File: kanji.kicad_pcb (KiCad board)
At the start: 2 copper layers, 105.3 x 70.8 mm, 35 parts, among them J3 E-Ink, Q1 AO3400A, U1 BH1750FVI-TR, U3 SHT4x, U4 XIAO-ESP32-S3-SMD

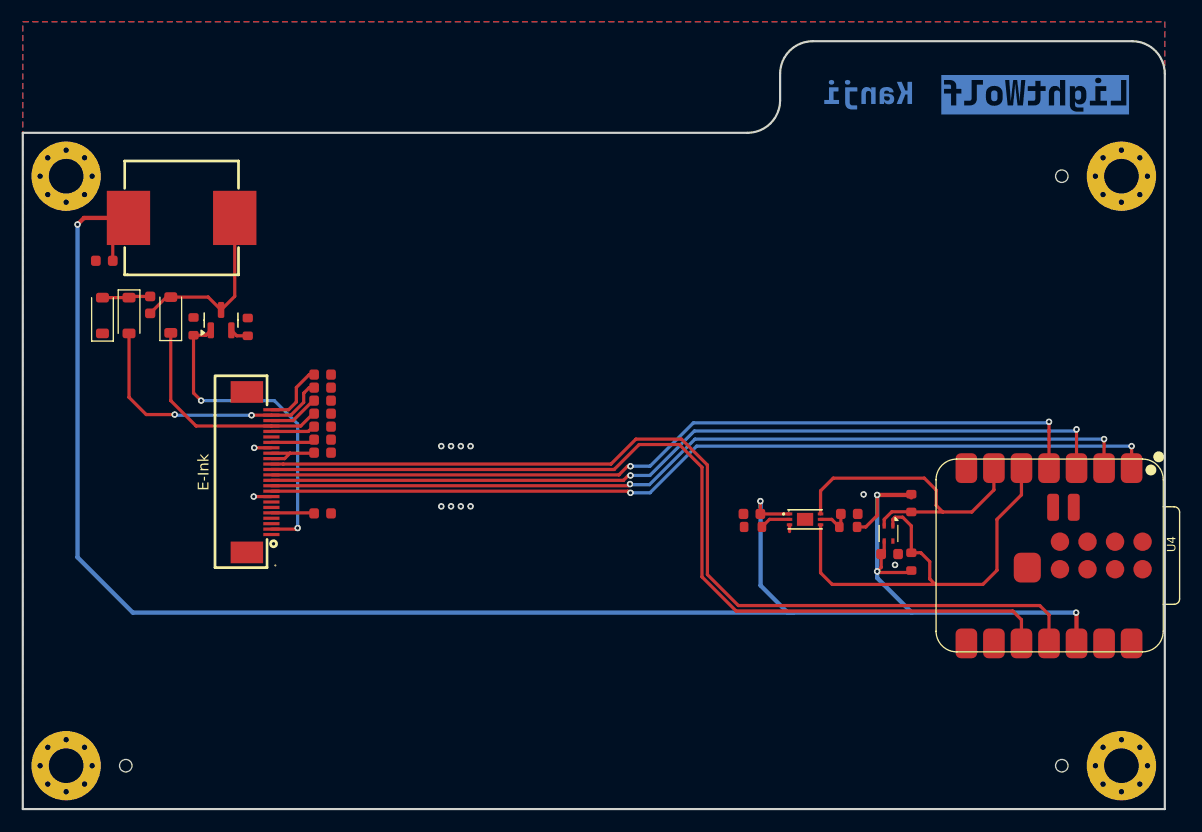
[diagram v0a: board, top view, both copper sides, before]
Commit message: feat: add case and update readme
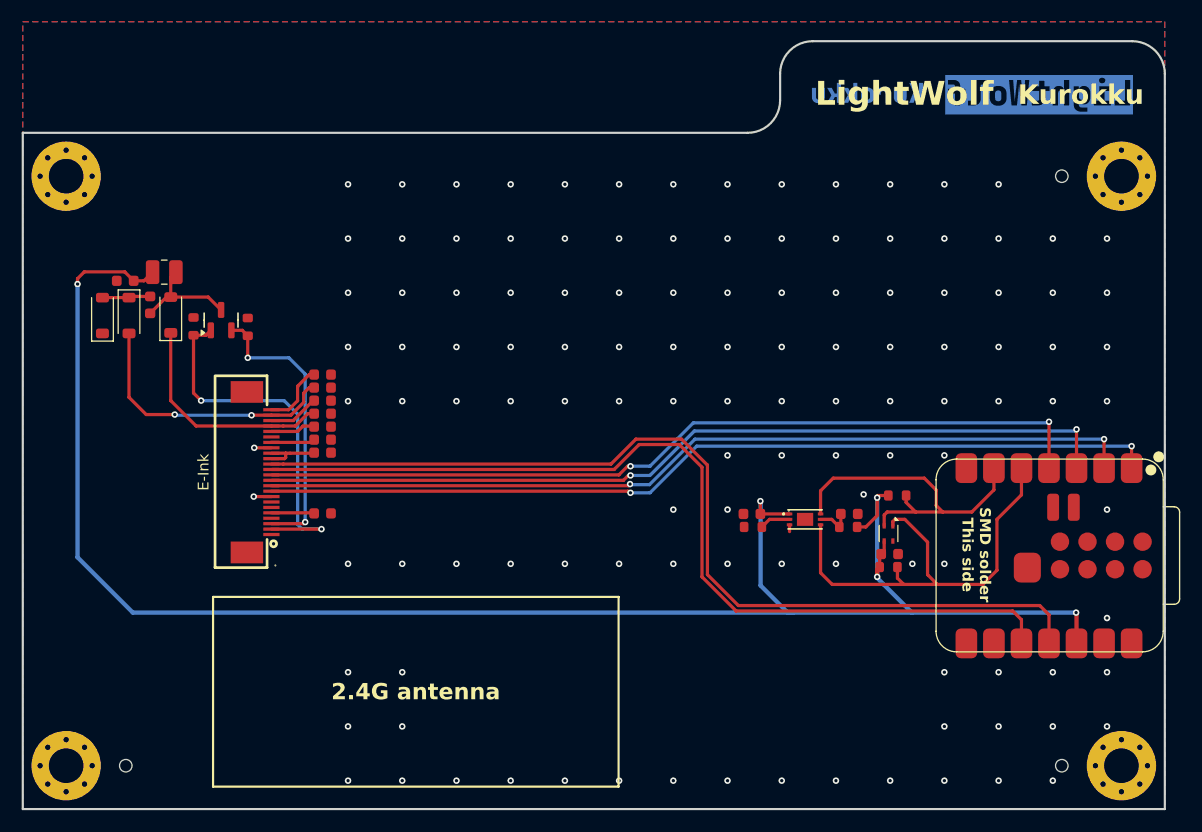
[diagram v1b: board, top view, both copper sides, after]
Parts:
- removed L1: CYL104R-47UH, easyeda2kicad:IND-SMD_L10.5-W10.5
- added L2: 10uH, Inductor_SMD:L_1008_2520Metric, F.Cu at (112.4, 75.8)
- R5: value 2.2Ω -> 3Ω
- R6: value 1MΩ -> 10kΩ
- moved C15 2.67 mm to (108.8, 76.6)
- moved R10 2.16 mm to (179.2, 103.0), turned to 0 degrees
- moved R9 1.48 mm to (180.0, 96.4), turned to 0 degrees
- turned R5 to -90 degrees
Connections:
- Q1 pad 2: Net-(Q1-S) -> /RDSE
- R5 pad 1: Net-(Q1-S) -> GND
- R5 pad 2: GND -> /RDSE
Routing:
- net /RDSE: track 0.00 -> 26.5 mm, vias 0 -> 2
- net +3V3: track 178.9 -> 166.9 mm
- net Net-(D2-A): track 16.7 -> 10.1 mm
- net /GDR: track 30.0 -> 34.7 mm
- net /SCL: track 29.9 -> 32.0 mm
- net Net-(Q1-S): track 1.72 -> 0.00 mm
- net /SDA: track 41.6 -> 42.9 mm
- net GND: vias 12 -> 123
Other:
- board text added: "2.4G antenna"
- board text added: "4.26″ E-Ink (10uH B/W)"
- board text added: "Kurokku"
- board text added: "LightWolf"
- board text added: "LightWolf Kurokku"
- board text added: "SMD solder This side"
- board text added: "Seeed Xiao ESP32-S3 (SMD)"
- board text added: "{ "ViaStitching": "0.2", "stitch_zone_0": { "HSpacing": "5", "VSpacing": "5", "HOffset": "0", "VOffset": "0", "Clearance": "0", "Randomize": false } }"
- board text added: "{ "ViaStitching": "0.2", "stitch_zone_0": { "HSpacing": "8", "VSpacing": "8", "HOffset": "0", "VOffset": "0", "Clearance": "0", "Randomize": false } }"
